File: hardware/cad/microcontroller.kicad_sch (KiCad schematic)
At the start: 51 parts, among them J401 6-440054-2, J402 6-440129-2, J403 2x2 PIN HEADER, J404 6-440054-2, J405 6-440129-2, J406 6-440054-2, J407 6-440129-2, J408 6-440054-2, J409 6-440129-2, Q401 DMN2050, Q402 DMN2050, SW401 FOOTSWITCH, SW402 FOOTSWITCH, U401 STM32G031K8U6

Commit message: started documentation
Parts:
- removed C18: 100nF, Capacitor_SMD:C_0402_1005Metric, symbol Device:C
- removed D201: RSB12JS2, Library:RSB12JS2, symbol Library:ROHM_RSB12JS2
- removed H401, H402, H403, H404: JLC_TOOLING_HOLE, Library:JLC_Tooling_hole, symbol Mechanical:MountingHole
- removed unit 1 of Q401
- removed Q402: DMN2050, Library:DMN2050LFDB, symbol Device:Q_Dual_NMOS_S1G1D2S2G2D1
- removed R404 (x3): 750Ω, Resistor_SMD:R_0402_1005Metric, symbol Device:R_US
- removed R405 (x5): 120Ω, Resistor_SMD:R_0402_1005Metric, symbol Device:R_US
- removed R410 (x2): 200Ω, Resistor_SMD:R_0402_1005Metric, symbol Device:R_US
- removed U401: STM32G031K8U6, Library:QFN-32-1EP_5x5mm_P0.5mm_EP3.45x3.45mm, symbol Library:STM32G031K8U6
- added C403, C409, C411, C412, C413, C414, C415, C416, C417, C418, C419, C420: 100n, symbol Device:C
- added C408, C410: 1u, symbol Device:C
- added D401: RSB12JS2, Library:RSB12JS2, symbol Library:ROHM_RSB12JS2
- added R419: 10k, symbol Device:R_US
- added R420, R421: 2.2k, symbol Device:R_US
- added R422, R423: 27.4, symbol Device:R_US
- added R424: 1k, symbol Device:R_US
- added SW403, SW404: SW_Push, symbol Switch:SW_Push
- added U401: PI4IOE5V6408, symbol Library:PI4IOE5V6408
- added U402: AT25xxx-MA, Package_DFN_QFN:DFN-8-1EP_3x2mm_P0.5mm_EP1.75x1.45mm, symbol Memory_EEPROM:AT25xxx-MA
- added U403: RP2040, Package_DFN_QFN:QFN-56-1EP_7x7mm_P0.4mm_EP3.2x3.2mm, symbol MCU_RaspberryPi:RP2040
- added Y401: Crystal_GND24, symbol Device:Crystal_GND24
- renumbered C38 to C401, C418 to C402, C38 to C404, C38 to C405, C418 to C406, C38 to C407, R404 to R401, R208 to R402, R405 to R407, R404 to R408, R507 to R409, R404 to R410, R208 to R411, R507 to R418
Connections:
- net +3V3: now also C403.1, C410.1, C411.1, C412.1, C413.1, C414.1, C415.1, C416.1, C417.1, C418.1, R419.1, U402.8 (VCC), U403.1 (IOVDD), U403.10 (IOVDD), U403.22 (IOVDD), U403.33 (IOVDD), U403.42 (IOVDD), U403.43 (ADC_AVDD), U403.44 (VREG_IN), U403.48 (USB_VDD), U403.49 (IOVDD)
- net +9V_EN: now also U403.6 (GPIO4)
- net -9V_EN: now also U403.7 (GPIO5)
- net GND: now also C403.2, C408.2, C409.2, C410.2, C411.2, C412.2, C413.2, C414.2, C415.2, C416.2, C417.2, C418.2, C419.1, C420.1, D401.2, D401.5, SW403.1, SW404.1, U402.4 (GND), U402.9 (GND), U403.19 (TESTEN), U403.57 (GND), Y401.2, Y401.4
- net SWDCK: now also J403.2 (Pin_2), D401.1, U403.24 (SWCLK); no longer J403.3 (Pin_3)
- net SWDIO: now also J403.3 (Pin_3), D401.4, U403.25 (SWD); no longer J403.2 (Pin_2)
- net SW_IN1: now also U403.12 (GPIO9)
- net SW_IN2: now also U403.13 (GPIO10)
- net SW_IN3: now also U403.14 (GPIO11)
- net SW_IN4: now also U403.15 (GPIO12)
- net ~{SW_EN}: now also U403.11 (GPIO8)
- net LEDB_EN: no longer names the net of R407.1
- new net: R420.1, SW403.2
- new net: R421.1, SW404.2
- new net: R421.2, U403.26 (RUN)
- new net: R423.2, U403.46 (USB_DM)
- new net: C420.2, R424.1, Y401.1
- new net: C419.2, U403.20 (XIN), Y401.3
- new net: R424.2, U403.21 (XOUT)
- new net: R422.2, U403.47 (USB_DP)
- new net +1V1: C408.1, C409.1, U403.23 (DVDD), U403.45 (VREG_VOUT), U403.50 (DVDD)
- new net DC_IN_PG: U403.8 (GPIO6)
- new net PG_3v3: U403.9 (GPIO7)
- new net QSPI_SCLK: U402.6 (SCK), U403.52 (QSPI_SCLK)
- new net QSPI_SD0: U402.5 (MOSI), U403.53 (QSPI_SD0)
- new net QSPI_SD1: U402.2 (MISO), U403.55 (QSPI_SD1)
- new net QSPI_SD2: U402.3 (~{WP}), U403.54 (QSPI_SD2)
- new net QSPI_SD3: U402.7 (~{HOLD}), U403.51 (QSPI_SD3)
- new net QSPI_SS: R419.2, R420.2, U402.1 (~{CS}), U403.56 (QSPI_SS)
- new net uC_USB_DM: R423.1
- new net uC_USB_DP: R422.1
- no-connect marks 17 -> 0
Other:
- note added: "100mA Current Draw"
- note added: "BOOT MODE"
- note added: "External flash memory up to 128 MBit Place as close as possible to microcontroller"
- note added: "MICROCONTROLLER"
- note added: "Place USB resistors close to microcontroller"
- note added: "RESET"
- note added: "Route as USB 2.0 Differential Pair"
- note added: "TODO Confirm bypass architecture"
- note removed: "I_PK = 27.5mA"
- note removed: "MECHANICAL"
- note removed: "MICROCONTROLLER AND SWITCHING"
- moved on the sheet: C401, C402, C404, C405, C406, D403, FID401, J401, J402, J404, J405, J406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

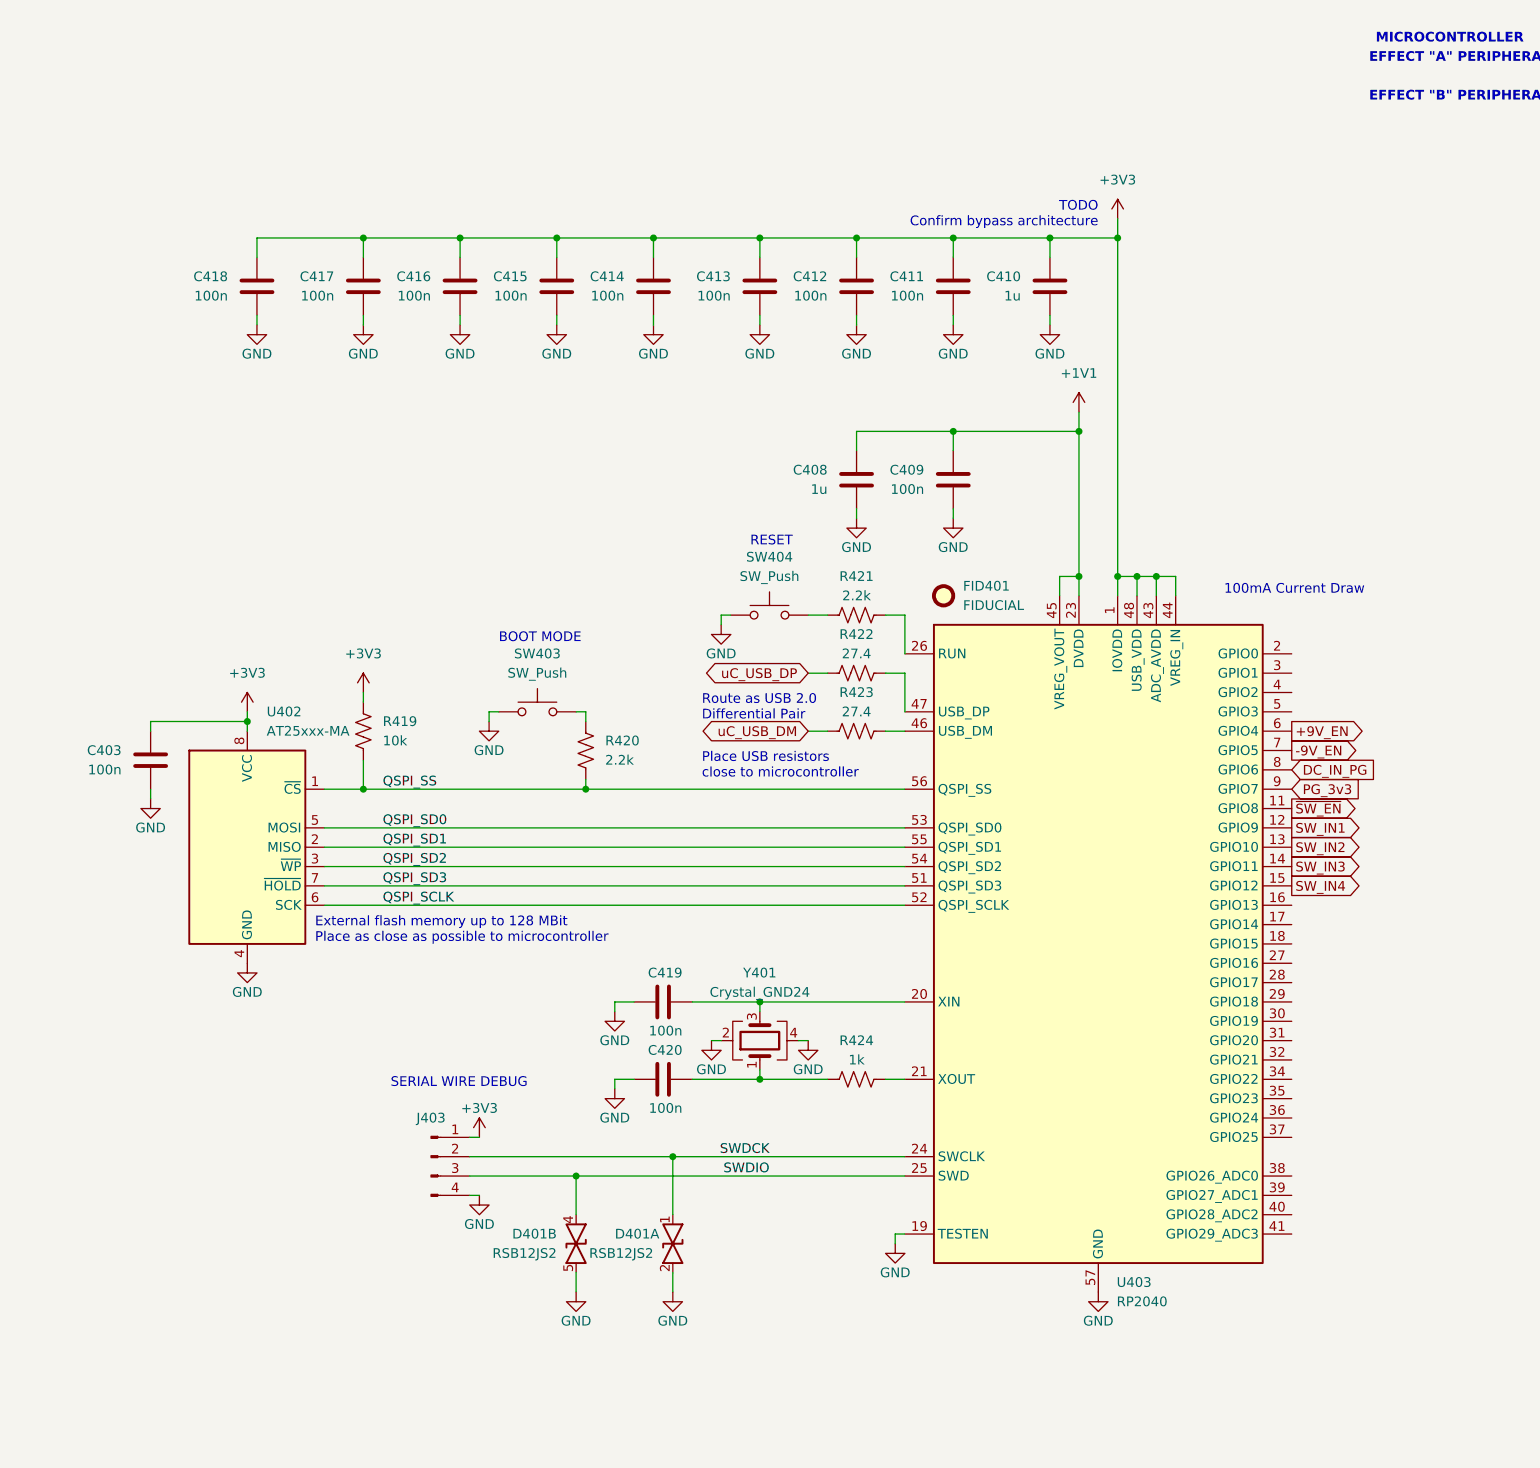
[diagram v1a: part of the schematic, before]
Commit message: minor changes before moving to new power supply topology
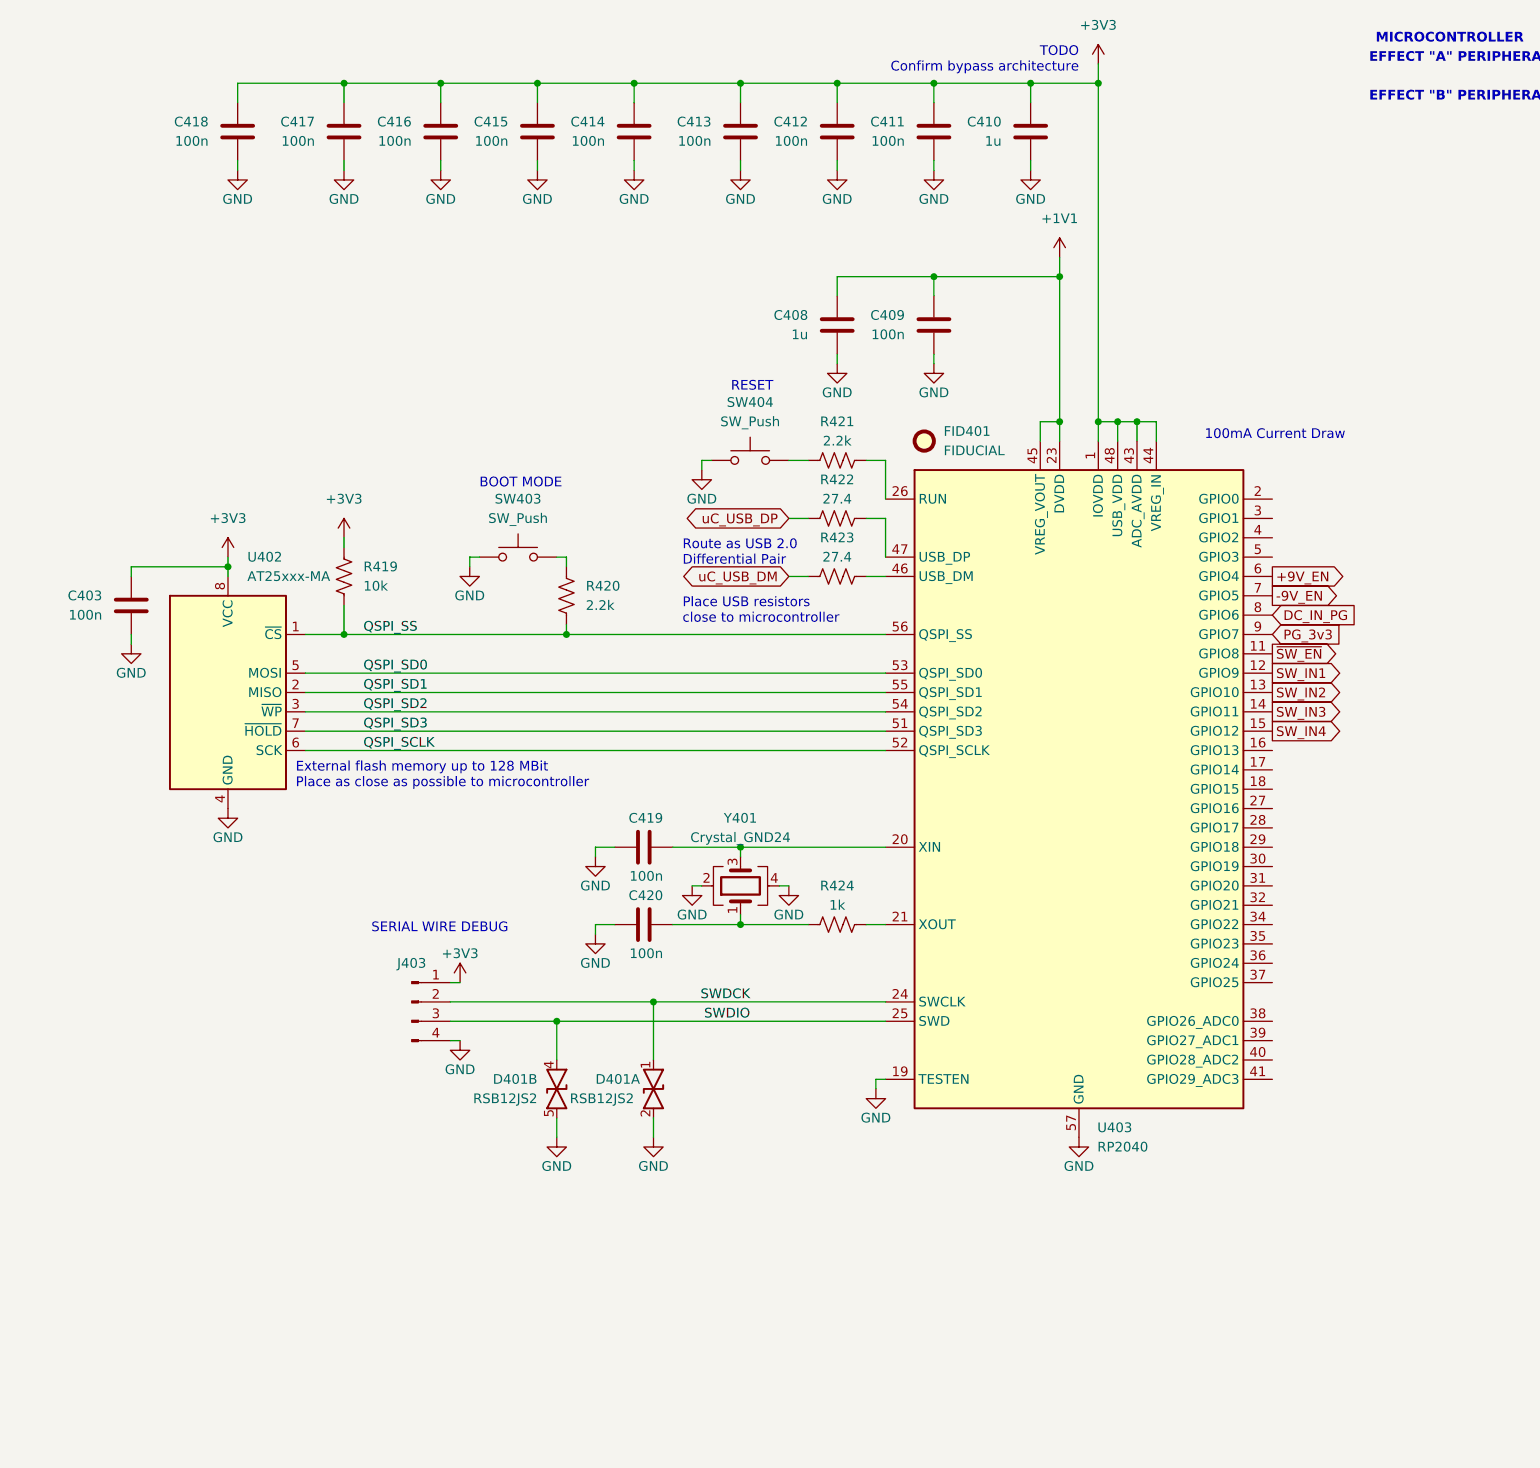
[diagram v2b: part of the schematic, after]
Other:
- moved on the sheet: C403, C408, C409, C410, C411, C412, C413, C414, C415, C416, C417, C418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

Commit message: cleanup
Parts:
- removed C401, C404, C405, C407: 100nF, Capacitor_SMD:C_0402_1005Metric, symbol Device:C
- removed C402, C406: 2.2μF, Capacitor_SMD:C_0603_1608Metric, symbol Device:C
- removed D404: RED LED, N/A, symbol Library:LED
- removed J401, J406, J408: 6-440054-2, Library:TE_HPI_2.0MM_PITCH_MALE_HEADER_2POS, symbol Connector:Conn_01x02_Pin
- removed J402, J405: 6-440129-2, N/A, symbol Connector:Conn_01x02_Socket
- removed Q401: DMN2050, Library:DMN2050LFDB, symbol Device:Q_Dual_NMOS_S1G1D2S2G2D1
- removed R401: 120Ω, Resistor_SMD:R_0402_1005Metric, symbol Device:R_US
- removed R402: 49.9kΩ, Resistor_SMD:R_0402_1005Metric, symbol Device:R_US
- removed R418: 15Ω, Resistor_SMD:R_0603_1608Metric, symbol Device:R_US
- removed SW401, SW402: FOOTSWITCH, N/A, symbol Switch:SW_SPST
- added C415, C416: 100n, symbol Device:C
- added C417, C418: 2.2μF, Capacitor_SMD:C_0603_1608Metric, symbol Device:C
- added C419, C420, C421, C422: 100nF, Capacitor_SMD:C_0402_1005Metric, symbol Device:C
- added D402: RED LED, N/A, symbol Library:LED
- added J402, J403, J405: 6-440054-2, Library:TE_HPI_2.0MM_PITCH_MALE_HEADER_2POS, symbol Connector:Conn_01x02_Pin
- added J406, J408: 6-440129-2, N/A, symbol Connector:Conn_01x02_Socket
- added R412: 15Ω, Resistor_SMD:R_0603_1608Metric, symbol Device:R_US
- added SW403, SW404: FOOTSWITCH, N/A, symbol Switch:SW_SPST
- R407: value 120Ω -> 49.9kΩ; Part Number RK73H1ETTP1200F -> RK73H1ETTP4992F
- R408: value 750Ω -> 49.9kΩ; Part Number RK73H1ETTP7500F -> RK73H1ETTP4992F
- R409: value 15Ω -> 120Ω; footprint Resistor_SMD:R_0603_1608Metric -> Resistor_SMD:R_0402_1005Metric; Part Number RK73H1JTTD15R0F -> RK73H1ETTP1200F
- R410: value 120Ω -> 15Ω; footprint Resistor_SMD:R_0402_1005Metric -> Resistor_SMD:R_0603_1608Metric; Part Number RK73H1ETTP1200F -> RK73H1JTTD15R0F
- R411: value 49.9kΩ -> 120Ω; Part Number RK73H1ETTP4992F -> RK73H1ETTP1200F
- renumbered C403 to C401, C418 to C402, C417 to C403, C416 to C404, C415 to C405, C414 to C406, C419 to C407, C420 to C408, C413 to C409, C412 to C410, C408 to C411, C411 to C412, C409 to C413, C410 to C414, J403 to J401, R419 to R401, R420 to R402, R421 to R403, R422 to R404, R423 to R405, R424 to R406, SW403 to SW401, SW404 to SW402, U402 to U401, U403 to U402, U401 to U403, W404 to W401, W403 to W402, W402 to W403, W401 to W404
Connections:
- net +3V3: now also J404.1 (Pin_1), C419.2, C420.2, C421.2, C422.2, J402.1 (Pin_1), J403.1 (Pin_1), J405.1 (Pin_1); no longer J404.2 (Pin_2)
- net GND: now also R407.1, R408.1, C417.1, C418.1, C419.1, C420.1, C421.1, C422.1; no longer R408.2, R411.1
- net VS_A: now also R410.2, U403.11 (P1)
- net VS_B: now also U403.7 (P3), R412.2; no longer R409.2
- net V_FTSW_FILT_A: now also R407.2, R409.2, U403.12 (P0), C417.2; no longer R410.2, R411.2
- net V_FTSW_FILT_B: now also R408.2, R411.2, U403.8 (P2), C418.2
- net V_FTSW_RAW_A: now also R409.1, J402.2 (Pin_2); no longer R410.1
- net V_FTSW_RAW_B: now also J404.2 (Pin_2), R411.1
- net V_LEDA: now also R410.1, J403.2 (Pin_2)
- net V_LEDB: now also J405.2 (Pin_2), R412.1; no longer J404.1 (Pin_1), R409.1
- net at J407.1 (Pin_1): now also D402.2 (A)
- net at J407.2 (Pin_2): now also D402.1 (K)
- net at J409.2 (Pin_2): now also D403.1 (K)
- net at J409.1 (Pin_1): now also D403.2 (A)
- removed net VG_LEDB: R407.2, R408.1
- new net: J406.1 (Pin_1), SW403.1 (A)
- new net: J406.2 (Pin_2), SW403.2 (B)
- new net: J408.1 (Pin_1), SW404.1 (A)
- new net: J408.2 (Pin_2), SW404.2 (B)
- no-connect marks 0 -> 4
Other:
- note added: "I2C BUS ADDRESS TABLE IO Expander: USB-C Port Controller:"
- note added: "INPUT"
- note added: "OUTPUT"
- moved on the sheet: D401A, D401B, U403, W401, W402, W403, W404
